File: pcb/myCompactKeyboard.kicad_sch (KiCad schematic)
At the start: 175 parts, among them J1 OLED_128x64, SW1 RotaryEncoder_Switch, SW2 RotaryEncoder_Switch, U1 Raspberry_Pi_Pico

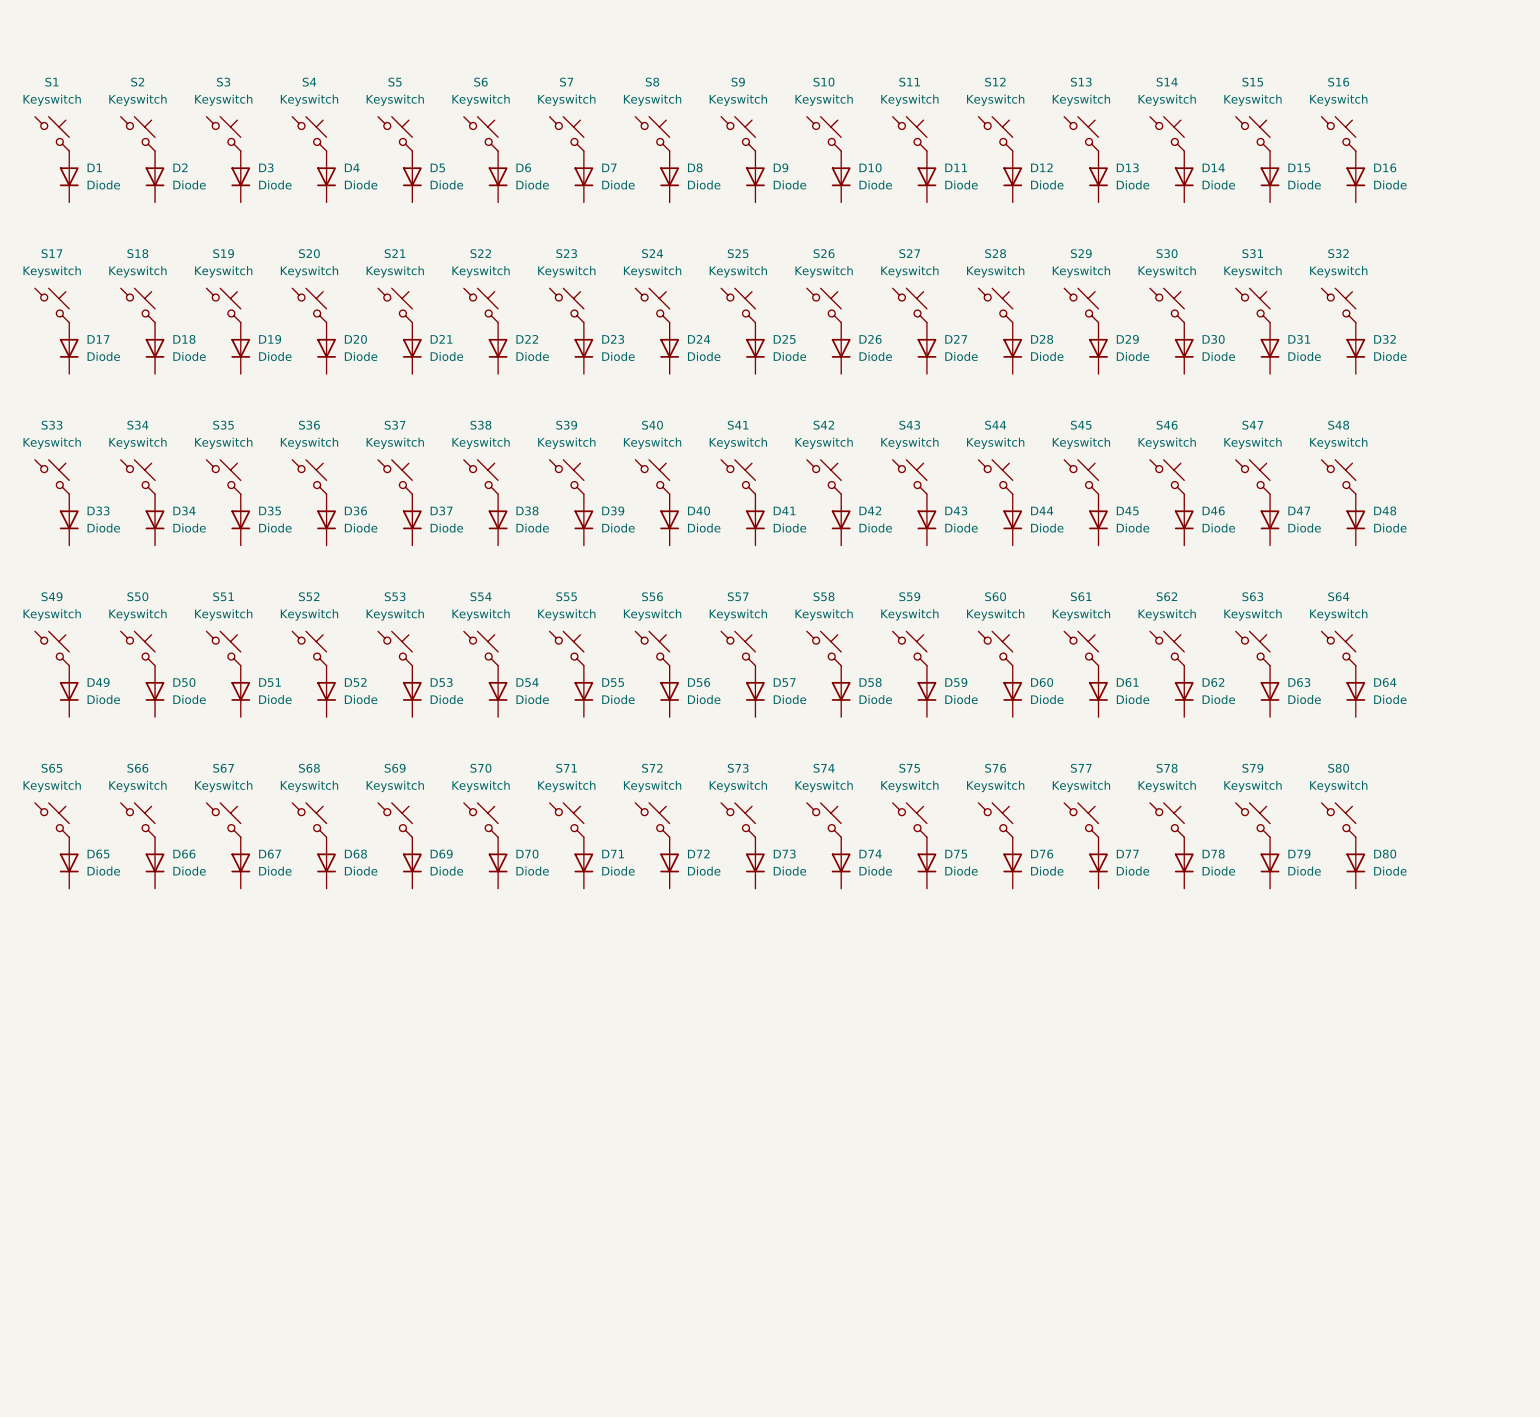
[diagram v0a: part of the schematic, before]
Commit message: switched layout to 8x12
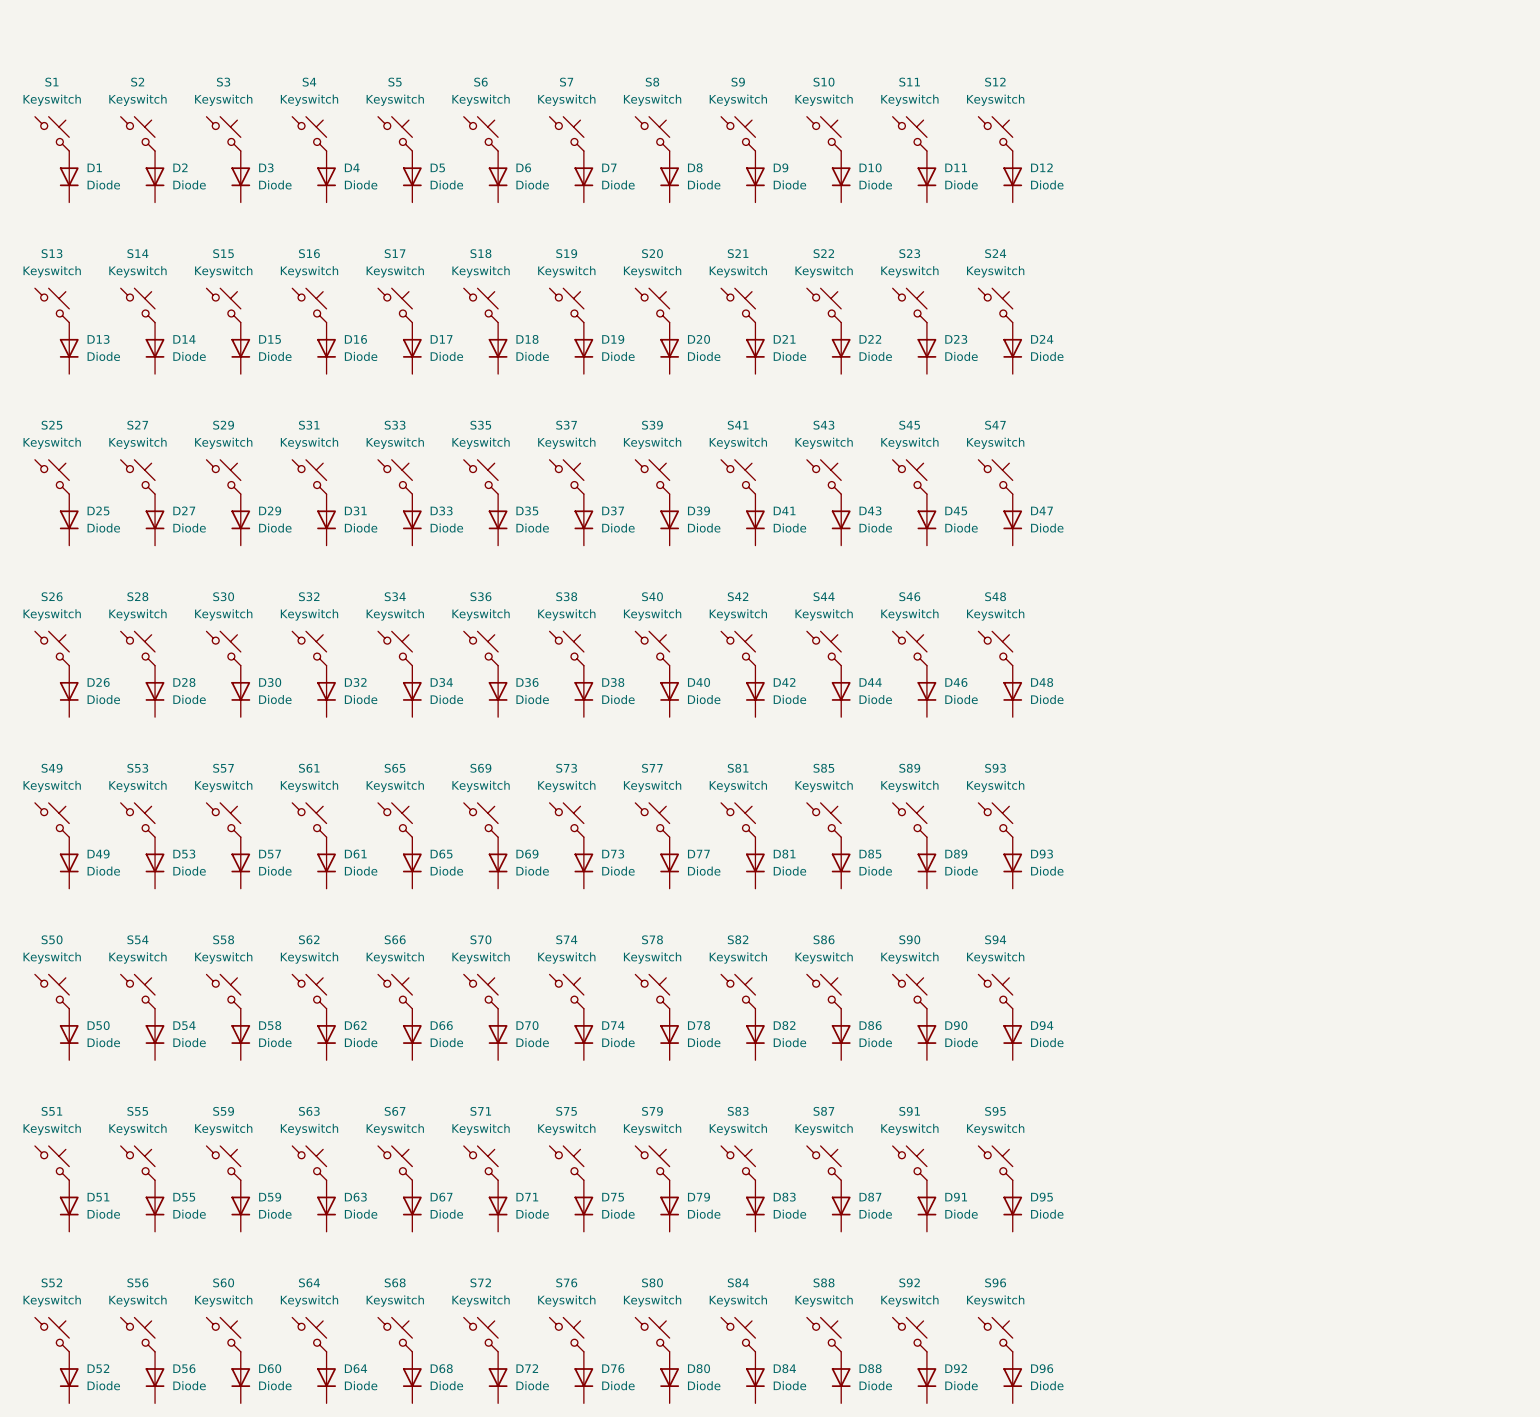
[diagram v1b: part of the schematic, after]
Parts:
- added D81, D82, D83, D84, D85, D86, D87, D88, D89, D90, D91, D92, D93, D94, D95, D96: Diode, ScottoKeebs_Components:Diode_DO-35, symbol ScottoKeebs:Placeholder_Diode
- added S81, S82, S83, S84, S85, S86, S87, S88, S89, S90, S91, S92, S93, S94, S95, S96: Keyswitch, ScottoKeebs_MX:MX_PCB_1.00u, symbol ScottoKeebs:Placeholder_Keyswitch
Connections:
- new net: D95.2 (A), S95.2
- new net: D94.2 (A), S94.2
- new net: D91.2 (A), S91.2
- new net: D84.2 (A), S84.2
- new net: D87.2 (A), S87.2
- new net: D81.2 (A), S81.2
- new net: D90.2 (A), S90.2
- new net: D83.2 (A), S83.2
- new net: D88.2 (A), S88.2
- new net: D93.2 (A), S93.2
- new net: D96.2 (A), S96.2
- new net: D89.2 (A), S89.2
- new net: D82.2 (A), S82.2
- new net: D86.2 (A), S86.2
- new net: D85.2 (A), S85.2
- new net: D92.2 (A), S92.2

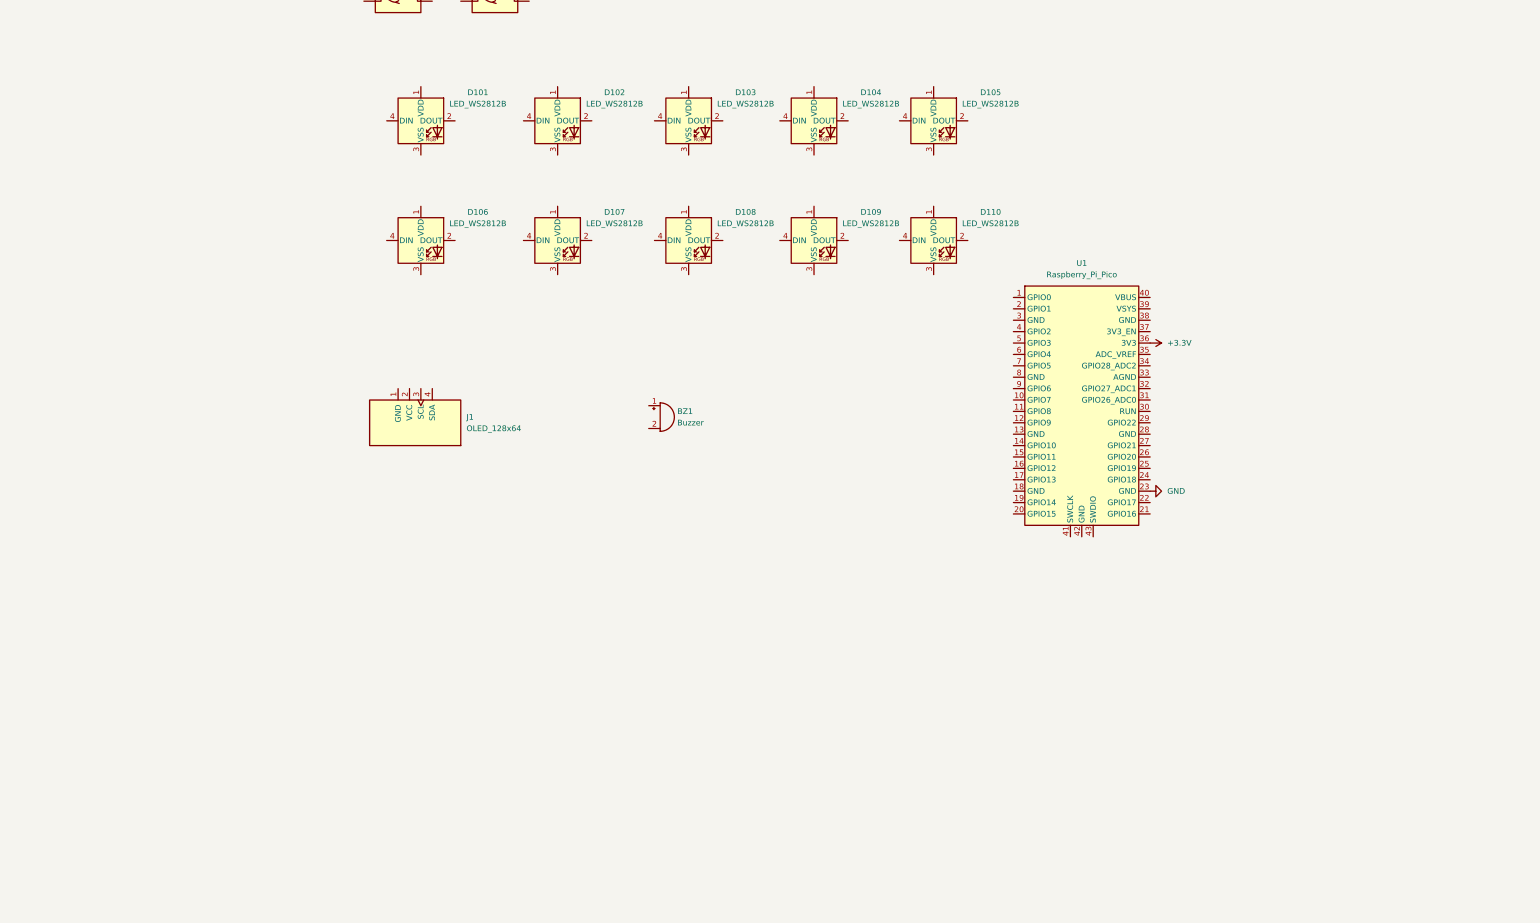
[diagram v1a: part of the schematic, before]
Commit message: added the led matrix to the schematic
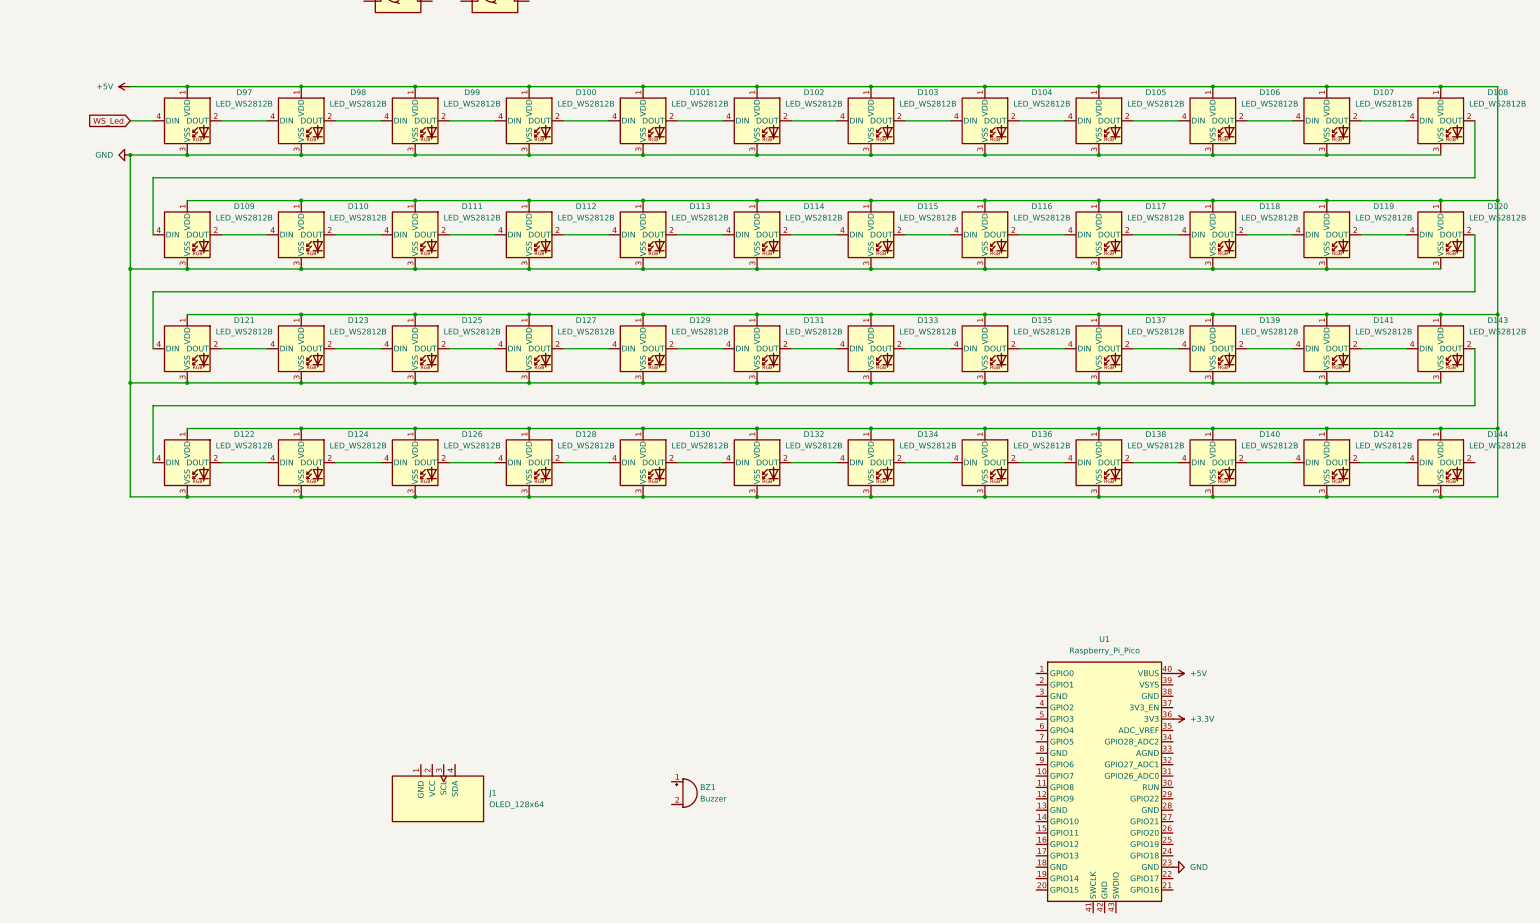
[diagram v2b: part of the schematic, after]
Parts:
- added D100, D111, D112, D113, D114, D115, D116, D117, D118, D119, D120, D121, D122, D123, D124, D125, D126, D127, D128, D129, D130, D131, D132, D133, D134, D135, D136, D137, D138, D139, D140, D141, D142, D143, D144, D97, D98, D99: LED_WS2812B, ScottoKeebs_Components:LED_WS2812B, symbol ScottoKeebs:LED_WS2812B
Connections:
- net GND is gone; now on net +5V: U1.23 (GND)
- net +5V: now reaches D108.1 (VDD)
- net +5V: now also D101.1 (VDD), D101.3 (VSS), D102.1 (VDD), D102.3 (VSS), D103.1 (VDD), D103.3 (VSS), D104.1 (VDD), D104.3 (VSS), D105.1 (VDD), D105.3 (VSS), D106.1 (VDD), D106.3 (VSS), D107.1 (VDD), D107.3 (VSS), D108.3 (VSS), D109.1 (VDD), D109.3 (VSS), D110.1 (VDD), D110.3 (VSS), U1.40 (VBUS), D100.1 (VDD), D100.3 (VSS), D111.1 (VDD), D111.3 (VSS), D112.1 (VDD), D112.3 (VSS), D113.1 (VDD), D113.3 (VSS), D114.1 (VDD), D114.3 (VSS), D115.1 (VDD), D115.3 (VSS), D116.1 (VDD), D116.3 (VSS), D117.1 (VDD), D117.3 (VSS), D118.1 (VDD), D118.3 (VSS), D119.1 (VDD), D119.3 (VSS), D120.1 (VDD), D120.3 (VSS), D121.1 (VDD), D121.3 (VSS), D122.1 (VDD), D122.3 (VSS), D123.1 (VDD), D123.3 (VSS), D124.1 (VDD), D124.3 (VSS), D125.1 (VDD), D125.3 (VSS), D126.1 (VDD), D126.3 (VSS), D127.1 (VDD), D127.3 (VSS), D128.1 (VDD), D128.3 (VSS), D129.1 (VDD), D129.3 (VSS), D130.1 (VDD), D130.3 (VSS), D131.1 (VDD), D131.3 (VSS), D132.1 (VDD), D132.3 (VSS), D133.1 (VDD), D133.3 (VSS), D134.1 (VDD), D134.3 (VSS), D135.1 (VDD), D135.3 (VSS), D136.1 (VDD), D136.3 (VSS), D137.1 (VDD), D137.3 (VSS), D138.1 (VDD), D138.3 (VSS), D139.1 (VDD), D139.3 (VSS), D140.1 (VDD), D140.3 (VSS), D141.1 (VDD), D141.3 (VSS), D142.1 (VDD), D142.3 (VSS), D143.1 (VDD), D143.3 (VSS), D144.1 (VDD), D144.3 (VSS), D97.1 (VDD), D97.3 (VSS), D98.1 (VDD), D98.3 (VSS), D99.1 (VDD), D99.3 (VSS)
- net at D108.2 (DOUT): now also D109.4 (DIN)
- net at D108.4 (DIN): now also D107.2 (DOUT)
- net at D104.2 (DOUT): now also D105.4 (DIN)
- net at D104.4 (DIN): now also D103.2 (DOUT)
- net at D103.4 (DIN): now also D102.2 (DOUT)
- net at D105.2 (DOUT): now also D106.4 (DIN)
- net at D101.2 (DOUT): now also D102.4 (DIN)
- net at D101.4 (DIN): now also D100.2 (DOUT)
- net at D109.2 (DOUT): now also D110.4 (DIN)
- net at D106.2 (DOUT): now also D107.4 (DIN)
- net at D110.2 (DOUT): now also D111.4 (DIN)
- new net: D133.2 (DOUT), D135.4 (DIN)
- new net: D131.2 (DOUT), D133.4 (DIN)
- new net: D121.2 (DOUT), D123.4 (DIN)
- new net: D120.2 (DOUT), D121.4 (DIN)
- new net: D125.2 (DOUT), D127.4 (DIN)
- new net: D123.2 (DOUT), D125.4 (DIN)
- new net: D111.2 (DOUT), D112.4 (DIN)
- new net: D140.2 (DOUT), D142.4 (DIN)
- new net: D138.2 (DOUT), D140.4 (DIN)
- new net: D139.2 (DOUT), D141.4 (DIN)
- new net: D137.2 (DOUT), D139.4 (DIN)
- new net: D141.2 (DOUT), D143.4 (DIN)
- new net: D128.2 (DOUT), D130.4 (DIN)
- new net: D126.2 (DOUT), D128.4 (DIN)
- new net: D119.2 (DOUT), D120.4 (DIN)
- new net: D118.2 (DOUT), D119.4 (DIN)
- new net: D112.2 (DOUT), D113.4 (DIN)
- new net: D136.2 (DOUT), D138.4 (DIN)
- new net: D134.2 (DOUT), D136.4 (DIN)
- new net: D98.2 (DOUT), D99.4 (DIN)
- new net: D97.2 (DOUT), D98.4 (DIN)
- new net: D117.2 (DOUT), D118.4 (DIN)
- new net: D116.2 (DOUT), D117.4 (DIN)
- new net: D130.2 (DOUT), D132.4 (DIN)
- new net: D100.4 (DIN), D99.2 (DOUT)
- new net: D135.2 (DOUT), D137.4 (DIN)
- new net: D129.2 (DOUT), D131.4 (DIN)
- new net: D127.2 (DOUT), D129.4 (DIN)
- new net: D142.2 (DOUT), D144.4 (DIN)
- new net: D132.2 (DOUT), D134.4 (DIN)
- new net: D122.2 (DOUT), D124.4 (DIN)
- new net: D122.4 (DIN), D143.2 (DOUT)
- new net: D124.2 (DOUT), D126.4 (DIN)
- new net: D114.2 (DOUT), D115.4 (DIN)
- new net: D113.2 (DOUT), D114.4 (DIN)
- new net: D115.2 (DOUT), D116.4 (DIN)
- new net WS_Led: D97.4 (DIN)
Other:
- moved on the sheet: BZ1, D101, J1, U1
